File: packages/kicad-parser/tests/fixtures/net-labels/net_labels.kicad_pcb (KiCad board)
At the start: 4 copper layers, 40 x 40 mm, 2 parts, among them J1 NetLabels_Back, U1 NetLabels_Front

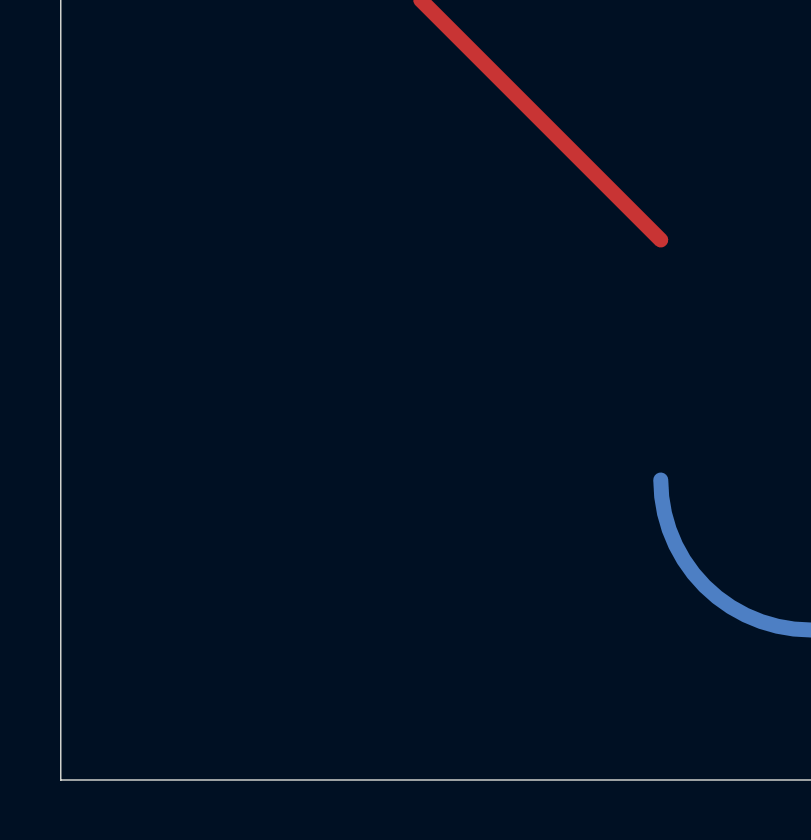
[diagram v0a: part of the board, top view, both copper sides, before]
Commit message: feat(board): net names inside filled zones
pcbnew shows a zone's net only in the tooltip; Altium labels its pours, and
the name of the copper under a component is exactly the context a reviewer
wants. Add a fourth label kind, zoneNetNames, off by default so the default
view still matches pcbnew.

Each filled polygon above a 0.6 mm inscribed-width floor gets one label at
its pole of inaccessibility (Mapbox's polylabel search over the signed
distance to the ring). The centroid of a ground pour with a cut-out lies in
the cut-out; the pole never does, and KiCad's fractured rings, with the
hole joined to the outline by a slit, work unchanged under even-odd
containment. Text is sized like a pad net name whose pad is the inscribed
circle, capped at 5 mm rather than KiCad's 10 mm so a wide pour does not
dominate, and stroked a little lighter than a pad label. Footprint zones
are transformed into board space as the painter draws them.

Labels sit on the copper's :X.Cu:NetNames layer, so they hide, dim and
isolate with it and draw above the fill. The fixture gains a fractured
GND pour and a sliver island.

Co-Authored-By: Claude Opus 5 <noreply@anthropic.com>
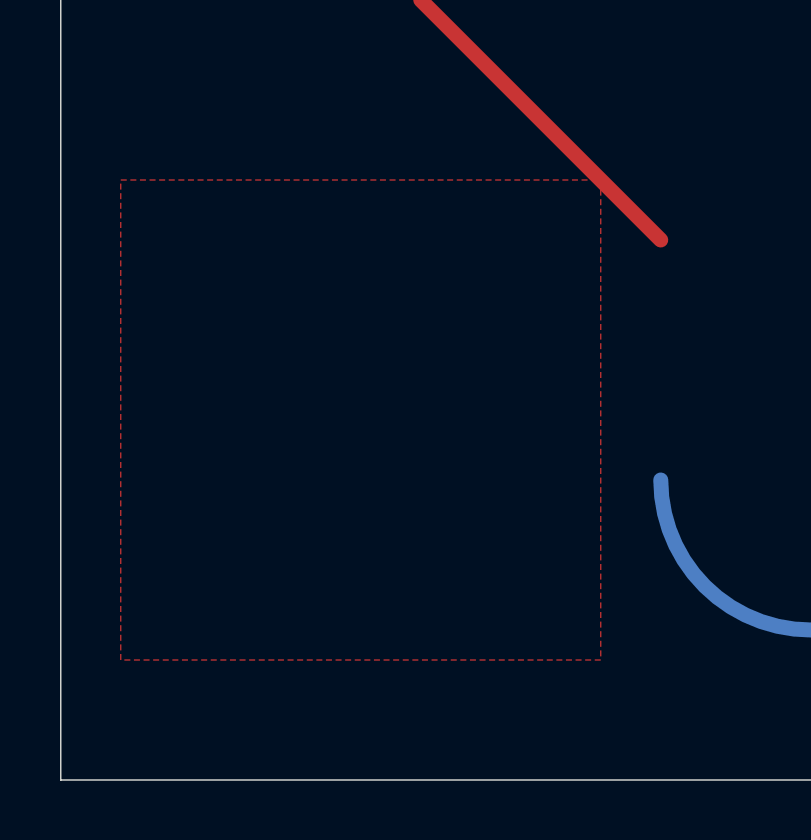
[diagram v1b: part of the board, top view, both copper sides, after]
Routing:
- added copper zone on F.Cu, net GND
